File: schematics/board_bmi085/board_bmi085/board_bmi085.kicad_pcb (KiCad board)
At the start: 2 copper layers, 17 parts, among them J1 Conn_01x08_Pin, J3 Conn_01x08_Pin

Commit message: a
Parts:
- R1, R2, R3, R4: footprint Resistor_SMD:R_0603_1608Metric -> Resistor_SMD:R_0402_1005Metric
- moved R13 16.5 mm to (120.0, 79.3)
- moved R12 15.0 mm to (120.0, 80.9)
- moved J1 15.0 mm to (116.3, 87.4)
- moved R14 9.68 mm to (120.0, 82.7), turned to 180 degrees
- moved J3 9.51 mm to (136.1, 87.5), turned to 180 degrees
- moved R15 7.45 mm to (120.0, 84.3), turned to 180 degrees
- moved R3 7.42 mm to (126.7, 78.7)
- moved R4 7.31 mm to (126.7, 79.7)
- moved R10 5.67 mm to (122.9, 82.8)
- moved R11 5.66 mm to (122.9, 81.8)
- moved R8 5.64 mm to (122.9, 80.8)
- moved R9 5.63 mm to (122.9, 79.8)
- moved R2 1.84 mm to (121.0, 87.1)
- moved R1 1.50 mm to (121.0, 86.1)
- moved C1 1.33 mm to (123.3, 85.1), turned to -90 degrees
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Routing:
- net VDD: track 46.2 -> 80.0 mm, vias 3 -> 6
- net /int_a: track 4.93 -> 28.9 mm, vias 0 -> 2
- net /int_b: track 8.38 -> 24.6 mm
- net Net-(R10-Pad2): track 18.4 -> 4.97 mm
- net Net-(U1-INT1): track 19.3 -> 9.52 mm
- net GND: track 58.1 -> 67.2 mm
- net Net-(U1-INT2): track 21.9 -> 13.2 mm
- net /scl: track 34.6 -> 42.5 mm, vias 0 -> 2
- net /sda: track 28.7 -> 35.5 mm, vias 0 -> 2
- net Net-(U1-INT3): track 8.75 -> 3.17 mm
- net Net-(U1-INT4): track 8.50 -> 3.23 mm
- net /addr_a: track 9.87 -> 5.93 mm
- net /addr_b: track 8.09 -> 6.42 mm, vias 0 -> 2
- added copper zone on B.Cu, net GND
- added copper zone on F.Cu, net GND
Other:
- board outline added: 19.8 x 13.2 mm

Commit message: a
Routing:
- net Net-(U1-INT2): track 13.2 -> 14.4 mm
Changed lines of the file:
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@@
+	)
+	(segment
+		(start 131.2 82)
+		(end 131.2 81.5)
+		(width 0.2)
+		(layer "F.Cu")
+		(net 11)
+	)
+	(segment
+		(start 131.1 82.1)
+		(end 131.2 82)
+		(width 0.2)
+		(layer "F.Cu")
+		(net 11)
+	)
+	(segment
+		(start 131.2 81.5)
+		(end 130.8 81.1)
+		(width 0.2)
+		(layer "F.Cu")
+		(net 11)
+	)
+	(segment
+		(start 124.7 77.5)
+		(end 123.38 78.82)
+		(width 0.2)
+		(layer "F.Cu")
+		(net 11)
+	)
+	(segment
+		(start 130.8 78.5)
+		(end 129.8 77.5)
+		(width 0.2)
+		(layer "F.Cu")
+		(net 11)
 	)
 	(segment
 		(start 123.38 78.82)
+		(end 123.38 79.8)
+		(width 0.2)
+		(layer "F.Cu")
+		(net 11)
+	)
+	(segment
+		(start 129.8 77.5)
 		(end 124.7 77.5)
 		(width 0.2)
@@
 	)
 	(segment
-		(start 124.7 77.5)
-		(end 129.8 77.5)
+		(start 130.8 81.1)
+		(end 130.8 78.5)
 		(width 0.2)
 		(layer "F.Cu")
@@
 	)
 	(segment
-		(start 130.6 81.4)
-		(end 129.9 82.1)
+		(start 129.9 82.1)
+		(end 131.1 82.1)
 		(width 0.2)
 		(layer "F.Cu")
@@
 	)
 	(segment
-		(start 129.8 77.5)
-		(end 130.6 78.3)
-		(width 0.2)
-		(layer "F.Cu")
-		(net 11)
-	)
-	(segment
-		(start 130.6 78.3)
-		(end 130.6 81.4)
-		(width 0.2)
-		(layer "F.Cu")
-		(net 11)
-	)
-	(segment
-		(start 123.38 79.8)
-		(end 123.38 78.82)
-		(width 0.2)
-		(layer "F.Cu")
-		(net 11)
-	)
-	(segment
-		(start 123.823696 83.5)
-		(end 123.923696 83.6)
+		(start 123.38 82.8)
+		(end 124.18 83.6)
 		(width 0.2)
 		(layer "F.Cu")
@@
 	)
 	(segment
-		(start 123.38 82.8)
-		(end 123.823696 83.243696)
-		(width 0.2)
-		(layer "F.Cu")
-		(net 12)
-	)
-	(segment
-		(start 123.823696 83.243696)
-		(end 123.823696 83.5)
-		(width 0.2)
-		(layer "F.Cu")
-		(net 12)
-	)
-	(segment
-		(start 123.923696 83.6)
+		(start 124.18 83.6)
 		(end 126.07 83.6)
 		(width 0.2)
@@
 	)
 	(segment
-		(start 125.068114 83.1)
+		(start 123.38 81.88)
+		(end 123.69 82.19)
+		(width 0.2)
+		(layer "F.Cu")
+		(net 13)
+	)
+	(segment
+		(start 123.706134 82.19)
+		(end 123.96 82.443866)
+		(width 0.2)
+		(layer "F.Cu")
+		(net 13)
+	)
+	(segment
+		(start 123.38 81.8)
+		(end 123.38 81.88)
+		(width 0.2)
+		(layer "F.Cu")
+		(net 13)
+	)
+	(segment
+		(start 123.96 82.46)
+		(end 124.6 83.1)
+		(width 0.2)
+		(layer "F.Cu")
+		(net 13)
+	)
+	(segment
+		(start 123.69 82.19)
+		(end 123.706134 82.19)
+		(width 0.2)
+		(layer "F.Cu")
+		(net 13)
+	)
+	(segment
+		(start 124.6 83.1)
 		(end 126.07 83.1)
 		(width 0.2)
@@
 	)
 	(segment
-		(start 124.7825 82.814386)
-		(end 125.068114 83.1)
+		(start 123.96 82.443866)
+		(end 123.96 82.46)
 		(width 0.2)
 		(layer "F.Cu")
-		(net 13)
-	)
-	(segment
-		(start 123.38 81.8)
-		(end 124.394386 82.814386)
-		(width 0.2)
-		(layer "F.Cu")
-		(net 13)
-	)
-	(segment
-		(start 124.394386 82.814386)
-		(end 124.7825 82.814386)
-		(width 0.2)
-		(layer "F.Cu")

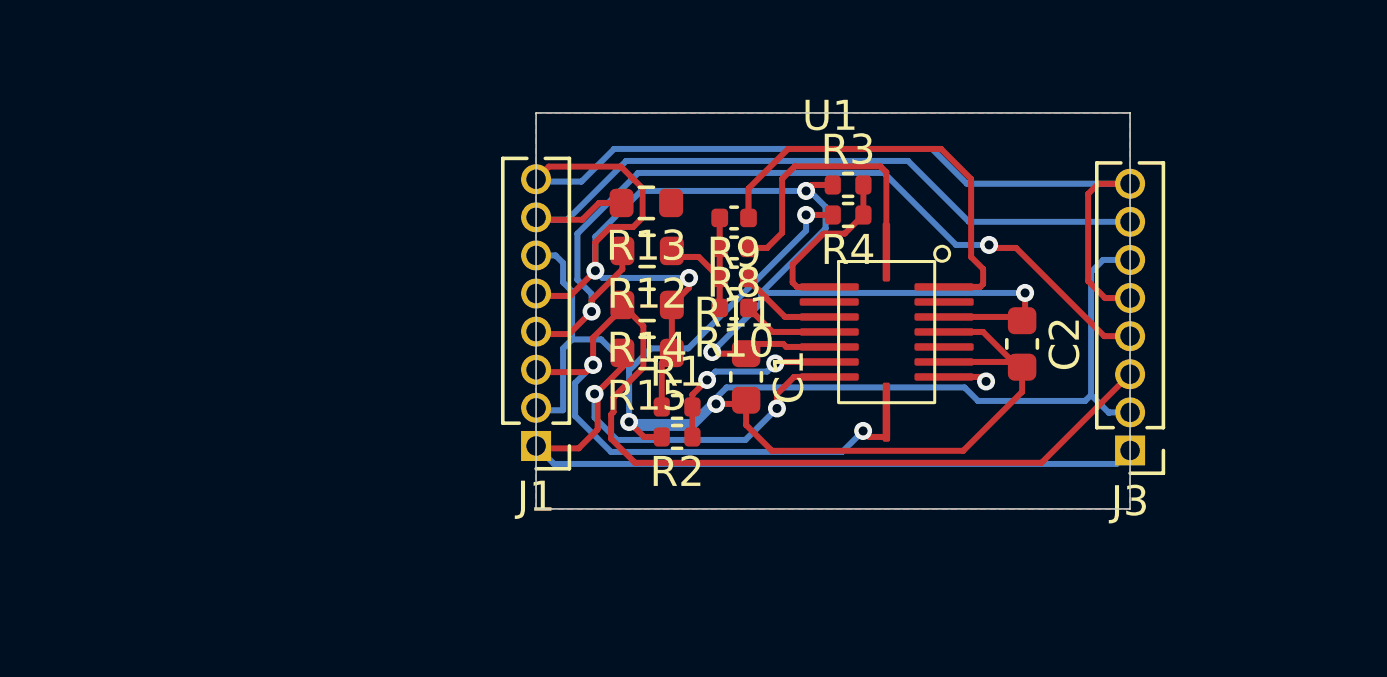
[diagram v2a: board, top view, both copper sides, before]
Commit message: Re-done the sensor board. Now it can be up 4 sensors on a single cable.
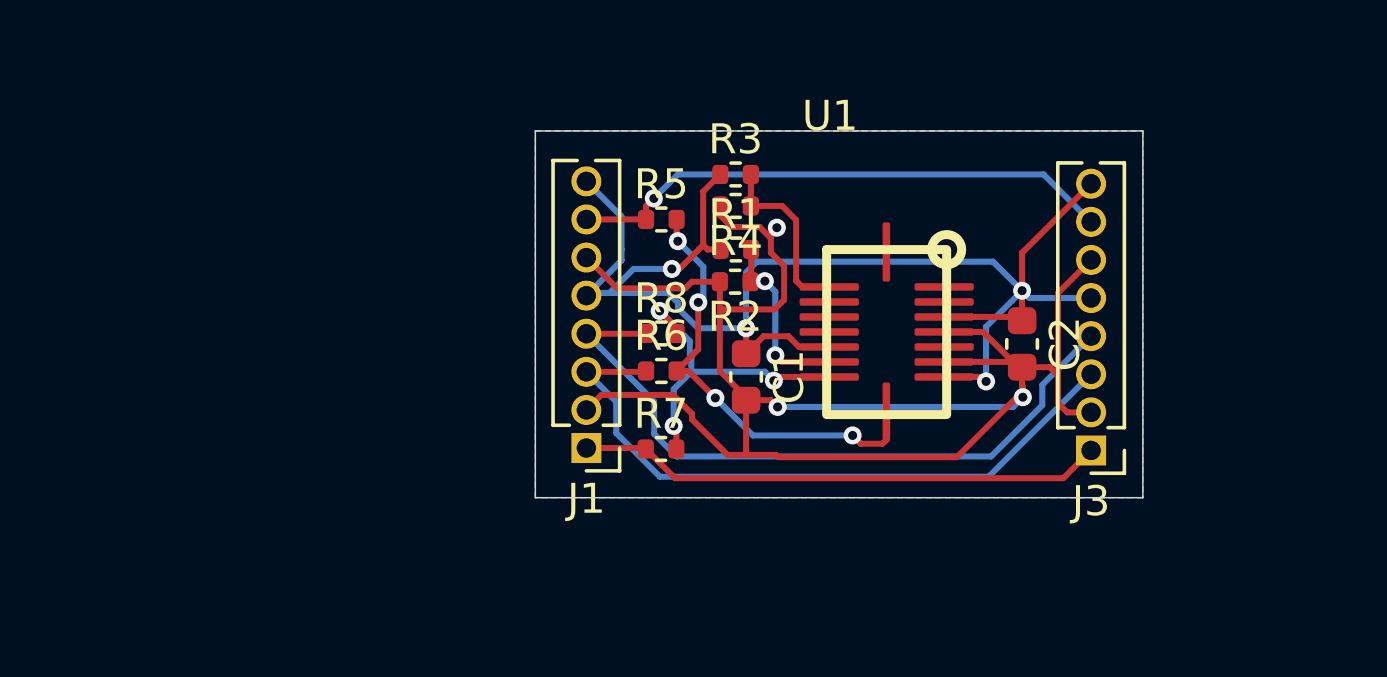
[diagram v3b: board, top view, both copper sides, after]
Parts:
- removed R10, R11, R9: 100, Capacitor_SMD:C_0402_1005Metric
- removed R12, R13: 100, Resistor_SMD:R_0603_1608Metric
- removed R14, R15: 2k, Resistor_SMD:R_0603_1608Metric
- added R5: 0, Resistor_SMD:R_0402_1005Metric, F.Cu at (120.5, 79.8)
- added R6: 0, Resistor_SMD:R_0402_1005Metric, F.Cu at (120.5, 84.9)
- added R7: 0, Resistor_SMD:R_0402_1005Metric, F.Cu at (120.5, 87.5)
- R1, R2, R3, R4: value 10k -> 0
- R8: value 100 -> 0; footprint Capacitor_SMD:C_0402_1005Metric -> Resistor_SMD:R_0402_1005Metric
- moved R1 5.60 mm to (123.0, 80.8)
- moved R2 5.52 mm to (122.9, 81.9)
- moved R3 3.77 mm to (123.0, 78.3)
- moved R4 3.76 mm to (123.0, 79.4)
- moved R8 3.74 mm to (120.5, 83.7), turned to 0 degrees
- moved J1 1.68 mm to (118.0, 87.5)
- moved J3 1.30 mm to (134.8, 87.5)
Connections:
- net /int_b renamed /scl_b
- J1 pad 1: /sda -> /sda_a
- J1 pad 3: /scl -> /scl_a
- J1 pad 4: /int_a -> /sda_b
- J3 pad 1: /sda -> /sda_a
- J3 pad 3: /scl -> /scl_a
- J3 pad 4: /int_a -> /sda_b
- R8 pad 1: Net-(U1-INT1) -> /sda_b
- R8 pad 2: Net-(R10-Pad2) -> /sda
- U1 pad 1: Net-(U1-INT2) -> unconnected-(U1-INT2-Pad1)
- U1 pad 12: Net-(U1-INT3) -> unconnected-(U1-INT3-Pad12)
- U1 pad 13: Net-(U1-INT4) -> unconnected-(U1-INT4-Pad13)
- U1 pad 16: Net-(U1-INT1) -> unconnected-(U1-INT1-Pad16)
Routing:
- net VDD: track 80.0 -> 50.2 mm, vias 6 -> 4
- net /int_a: track 28.9 -> 0.00 mm, vias 2 -> 0
- net /scl: track 42.5 -> 15.6 mm, vias 2 -> 4
- net /sda: track 35.5 -> 11.1 mm, vias 2 -> 3
- net /sda_b: track 0.00 -> 23.2 mm
- net /scl_a: track 0.00 -> 22.3 mm
- net /sda_a: track 0.00 -> 17.6 mm
- net Net-(U1-INT2): track 14.4 -> 0.00 mm
- net Net-(U1-INT1): track 9.52 -> 0.00 mm
- net GND: track 67.2 -> 59.6 mm
- net /scl_b: track 24.6 -> 18.4 mm, vias 0 -> 1
- net Net-(R10-Pad2): track 4.97 -> 0.00 mm
- net Net-(U1-INT4): track 3.28 -> 0.00 mm
- net Net-(U1-INT3): track 3.02 -> 0.00 mm
- net /addr_a: track 5.93 -> 5.00 mm
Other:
- board size 19.8 x 13.2 mm -> 20.2 x 12.2 mm

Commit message: Little tail is not needed.
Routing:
- net VDD: track 50.2 -> 49.6 mm
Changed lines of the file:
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@@
-	)
-	(segment
-		(start 123.3 84.099655)
-		(end 123.3 83.475)
-		(width 0.2)
-		(layer "B.Cu")
-		(net 1)
 	)
 	(segment

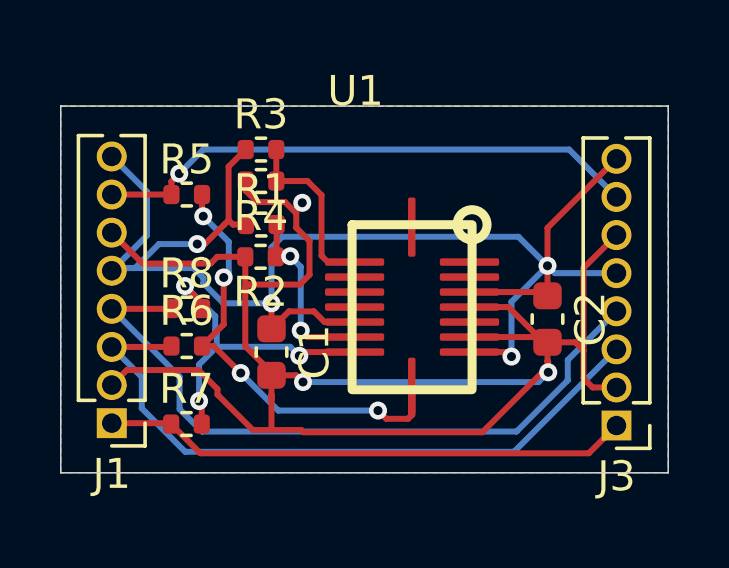
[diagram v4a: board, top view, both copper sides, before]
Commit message: Slightly re-routed wires so that through power and ground do not go through the IMU chip. Instead, they go around.
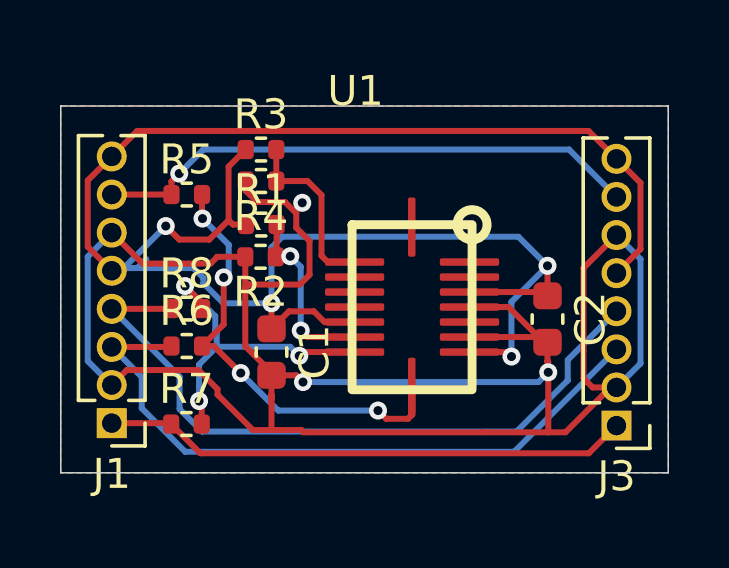
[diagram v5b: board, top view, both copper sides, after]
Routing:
- net VDD: track 49.6 -> 65.5 mm
- net GND: track 59.6 -> 73.8 mm
